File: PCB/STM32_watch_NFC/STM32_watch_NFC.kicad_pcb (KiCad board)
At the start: 4 copper layers, 37 x 37 mm, 119 parts, among them J1 Conn_01x06_Socket, J2 USB_C_Receptacle_PowerOnly_6P, Q1 2N7000, SW1 SW_DPST_x2, SW2 SW_DPST_x2, SW3 SW_DPST_x2, U1 STM32L031G6Ux, U2 MIC5365-3.3YC5, U3 TM1637, U4 MT3608, U5 BH1750FVI-TR, Y2 32.768kHz

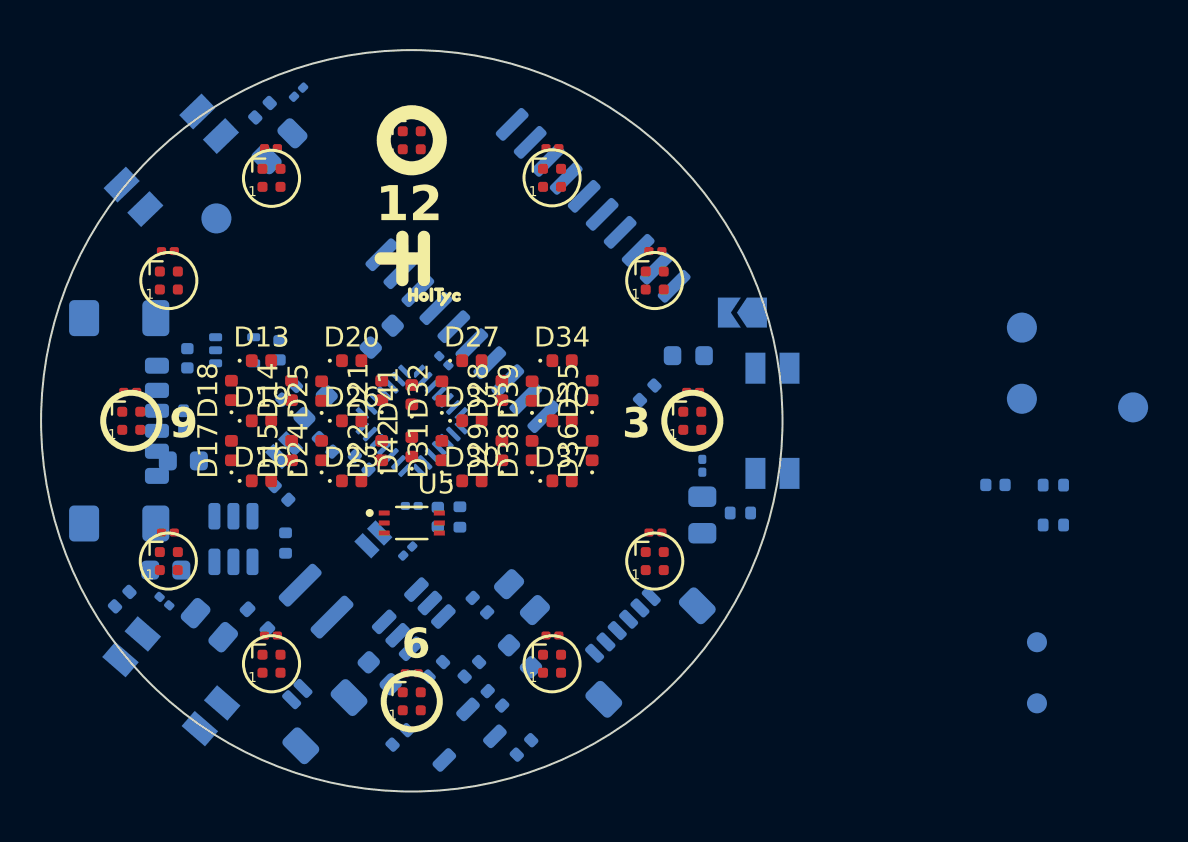
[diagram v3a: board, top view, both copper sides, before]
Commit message: TM1637 - in next commit I will delete the driver and connect the leds directly through matrix
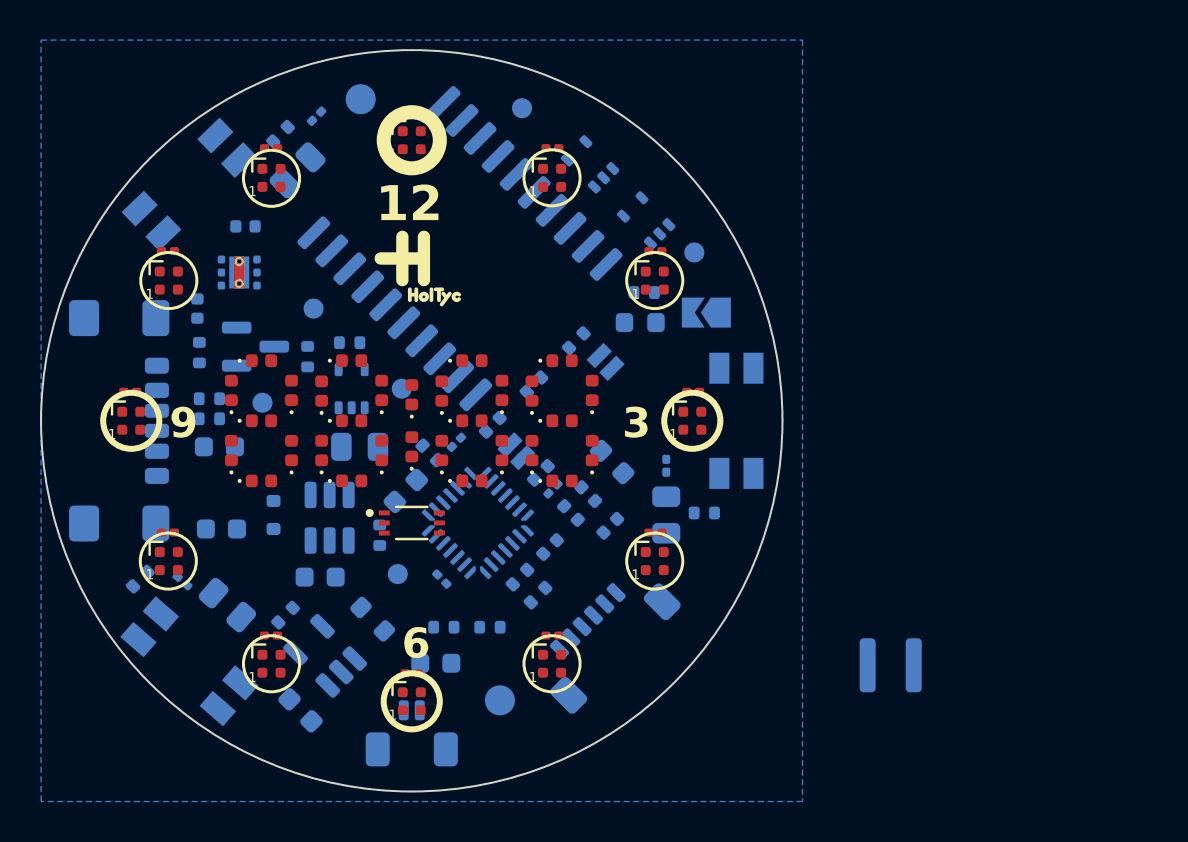
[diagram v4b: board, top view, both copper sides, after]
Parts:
- removed 3V3: 3V3, TestPoint:TestPoint_Pad_D1.5mm
- removed 5V1: 5V, TestPoint:TestPoint_Pad_D1.5mm
- removed C25: 10u, Capacitor_SMD:C_0603_1608Metric
- removed DINLED1, DINSTM2: ~, TestPoint:TestPoint_Pad_D1.0mm
- removed ME4055A1: ~, Package_TO_SOT_SMD:SOT-23-6
- removed U2: MIC5365-3.3YC5, Package_TO_SOT_SMD:SOT-353_SC-70-5
- added C32: 4.7uF, Capacitor_SMD:C_0603_1608Metric, B.Cu at (142.9, 119.4)
- added C33: 4.7uF, Capacitor_SMD:C_0603_1608Metric, B.Cu at (149.7, 117.1)
- added CLK: ~, TestPoint:TestPoint_Pad_D1.0mm, B.Cu at (162.6, 96.6)
- added DIO: ~, TestPoint:TestPoint_Pad_D1.0mm, B.Cu at (154.0, 89.4)
- added DLED: ~, TestPoint:TestPoint_Pad_D1.0mm, B.Cu at (148.0, 103.4)
- added DSTM: ~, TestPoint:TestPoint_Pad_D1.0mm, B.Cu at (141.1, 104.1)
- added R19: 5K1, Resistor_SMD:R_0402_1005Metric, B.Cu at (142.2, 114.7)
- added R22: 10k, Resistor_SMD:R_0603_1608Metric, B.Cu at (146.6, 114.9)
- added R23: 10K, Resistor_SMD:R_0402_1005Metric, B.Cu at (137.9, 101.6)
- added SCL: ~, TestPoint:TestPoint_Pad_D1.0mm, B.Cu at (147.8, 112.7)
- added SDA: ~, TestPoint:TestPoint_Pad_D1.0mm, B.Cu at (143.6, 99.4)
- added U10: LP5912-3.3DRV, Package_SON:WSON-6-1EP_2x2mm_P0.65mm_EP1x1.6mm_ThermalVias, B.Cu at (139.9, 97.6)
- added U6: MCP73831-3-OT, Package_TO_SOT_SMD:SOT-23-5, B.Cu at (144.2, 116.7)
- added U7: 74AHCT1G125, Package_TO_SOT_SMD:SOT-353_SC-70-5, B.Cu at (145.5, 103.4)
- added U8: 74AHCT1G125, Package_TO_SOT_SMD:SOT-353_SC-70-5, B.Cu at (160.2, 95.0)
- added U9: 74AHCT1G125, Package_TO_SOT_SMD:SOT-353_SC-70-5, B.Cu at (157.4, 92.2)
- L1: footprint Components:SLW3015 -> Inductor_SMD:L_Sunlord_SWPA3015S
- Q1: value 2N7000 -> BSS138; footprint Package_TO_SOT_SMD:TSOT-23 -> Package_TO_SOT_SMD:SOT-23
- R1, R2: value 10K -> 510
- R7: value 5K1 -> 10K
- moved GND 41.5 mm to (145.9, 89.0)
- moved +BAT 32.0 mm to (152.9, 119.0)
- moved L1 28.9 mm to (172.4, 117.2), turned to 180 degrees
- moved R21 26.7 mm to (153.9, 112.8), turned to -135 degrees
- moved R20 26.3 mm to (154.8, 113.7), turned to 45 degrees
- moved C31 22.4 mm to (155.4, 111.3), turned to 45 degrees
- moved Q1 22.3 mm to (140.7, 101.3), turned to 0 degrees
- moved R2 20.5 mm to (156.7, 101.0), turned to 45 degrees
- moved R6 19.9 mm to (145.4, 101.1), turned to 0 degrees
- moved C27 16.2 mm to (139.0, 110.4), turned to 180 degrees
- moved R1 15.8 mm to (154.6, 103.2), turned to -135 degrees
- moved C5 15.8 mm to (157.3, 108.7), turned to 135 degrees
- moved FB1 15.1 mm to (158.5, 107.1), turned to -45 degrees
- moved Y2 12.4 mm to (155.9, 104.3), turned to 45 degrees
- moved C8 11.1 mm to (152.5, 105.2), turned to 45 degrees
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- renumbered +BAT1 to +BAT, GND1 to GND
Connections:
- D13 pad 1: GRID1 -> A
- D13 pad 2: A -> GRID1
- D14 pad 1: GRID1 -> B
- D14 pad 2: B -> GRID1
- D15 pad 1: GRID1 -> C
- D15 pad 2: C -> GRID1
- D16 pad 1: GRID1 -> D
- D16 pad 2: D -> GRID1
- D17 pad 1: GRID1 -> E
- D17 pad 2: E -> GRID1
- D18 pad 1: GRID1 -> F
- D18 pad 2: F -> GRID1
- D19 pad 1: GRID1 -> G
- D19 pad 2: G -> GRID1
- D20 pad 1: GRID2 -> A
- D20 pad 2: A -> GRID2
- D21 pad 1: GRID2 -> B
- D21 pad 2: B -> GRID2
- D22 pad 1: GRID2 -> C
- D22 pad 2: C -> GRID2
- D23 pad 1: GRID2 -> D
- D23 pad 2: D -> GRID2
- D24 pad 1: GRID2 -> E
- D24 pad 2: E -> GRID2
- D25 pad 1: GRID2 -> F
- D25 pad 2: F -> GRID2
- D26 pad 1: GRID2 -> G
- D26 pad 2: G -> GRID2
- D27 pad 1: GRID3 -> A
- D27 pad 2: A -> GRID3
- D28 pad 1: GRID3 -> B
- D28 pad 2: B -> GRID3
- D29 pad 1: GRID3 -> C
- D29 pad 2: C -> GRID3
- D30 pad 1: GRID3 -> D
- D30 pad 2: D -> GRID3
- D31 pad 1: GRID3 -> E
- D31 pad 2: E -> GRID3
- D32 pad 1: GRID3 -> F
- D32 pad 2: F -> GRID3
- D33 pad 1: GRID3 -> G
- D33 pad 2: G -> GRID3
- D34 pad 1: GRID4 -> A
- D34 pad 2: A -> GRID4
- D35 pad 1: GRID4 -> B
- D35 pad 2: B -> GRID4
- D36 pad 1: GRID4 -> C
- D36 pad 2: C -> GRID4
- D37 pad 1: GRID4 -> D
- D37 pad 2: D -> GRID4
- D38 pad 1: GRID4 -> E
- D38 pad 2: E -> GRID4
- D39 pad 1: GRID4 -> F
- D39 pad 2: F -> GRID4
- D40 pad 1: GRID4 -> G
- D40 pad 2: G -> GRID4
- D41 pad 1: GND -> Net-(D41-K)
- D42 pad 1: GND -> Net-(D42-K)
- Q1 pad 1: DIN_STM -> VBUS
- Q1 pad 2: +3.3V -> GND
- Q1 pad 3: DIN_LED -> CHRG_STM
- R1 pad 1: +3.3V -> GND
- R1 pad 2: DIN_STM -> Net-(D42-K)
- R2 pad 1: +5V -> Net-(D41-K)
- R2 pad 2: DIN_LED -> GND
- R6 pad 1: DIN_STM -> DIN_LED
- R7 pad 1: Net-(ME4055A1-PROG) -> +3.3V
- R7 pad 2: GND -> CHRG_STM
- U1 pad 13: unconnected-(U1-PA7-Pad13) -> CLK_TM_STM
- U1 pad 14: unconnected-(U1-PB0-Pad14) -> DIO_TM_STM
- U3 pad 17: unconnected-(U3-DIO-Pad17) -> DIO_TM
- U3 pad 18: unconnected-(U3-CLK-Pad18) -> CLK_TM
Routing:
- added copper zone on B.Cu, net GND
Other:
- board text added: "Rev.B.1"
- board text removed: "+"
- board text removed: "Rev.B.0"

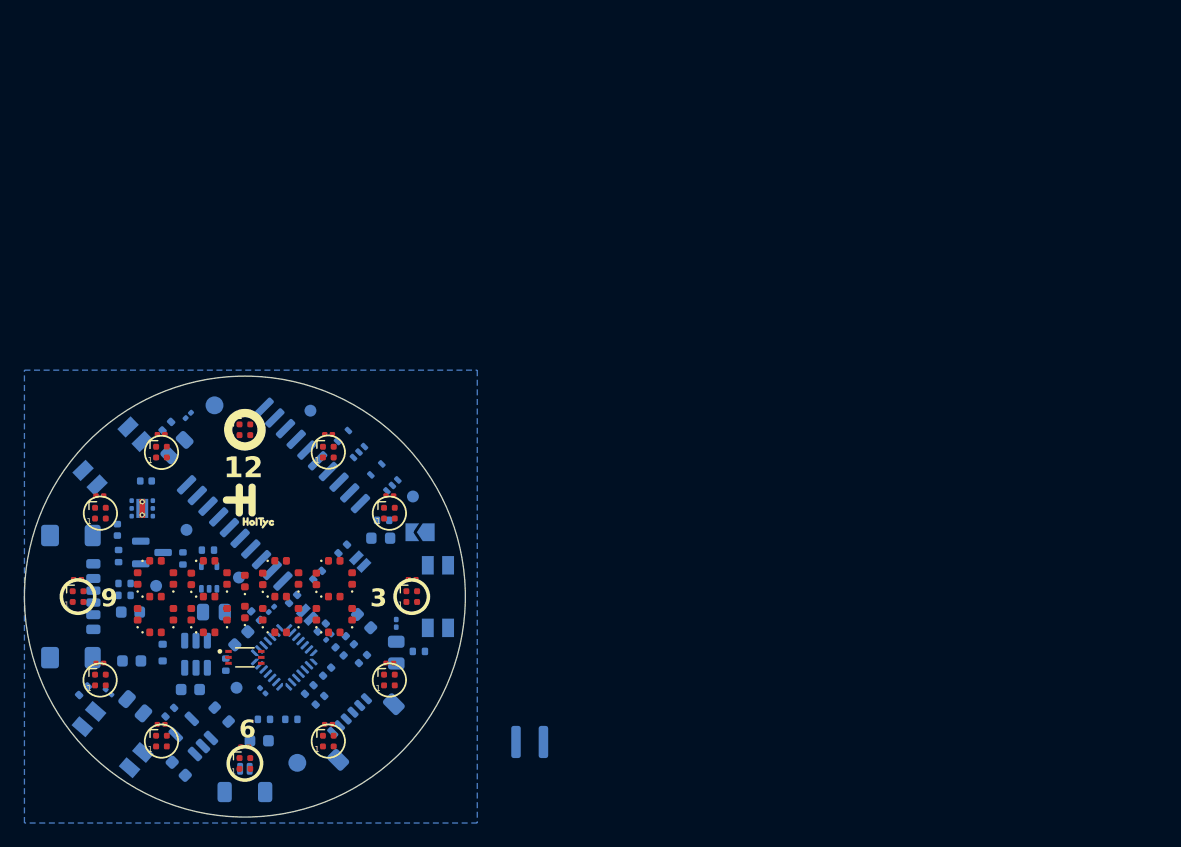
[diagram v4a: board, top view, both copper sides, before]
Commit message: Kicad/STM - new Routing 6
Version before Boston to work on it there - needs to replace every component :(
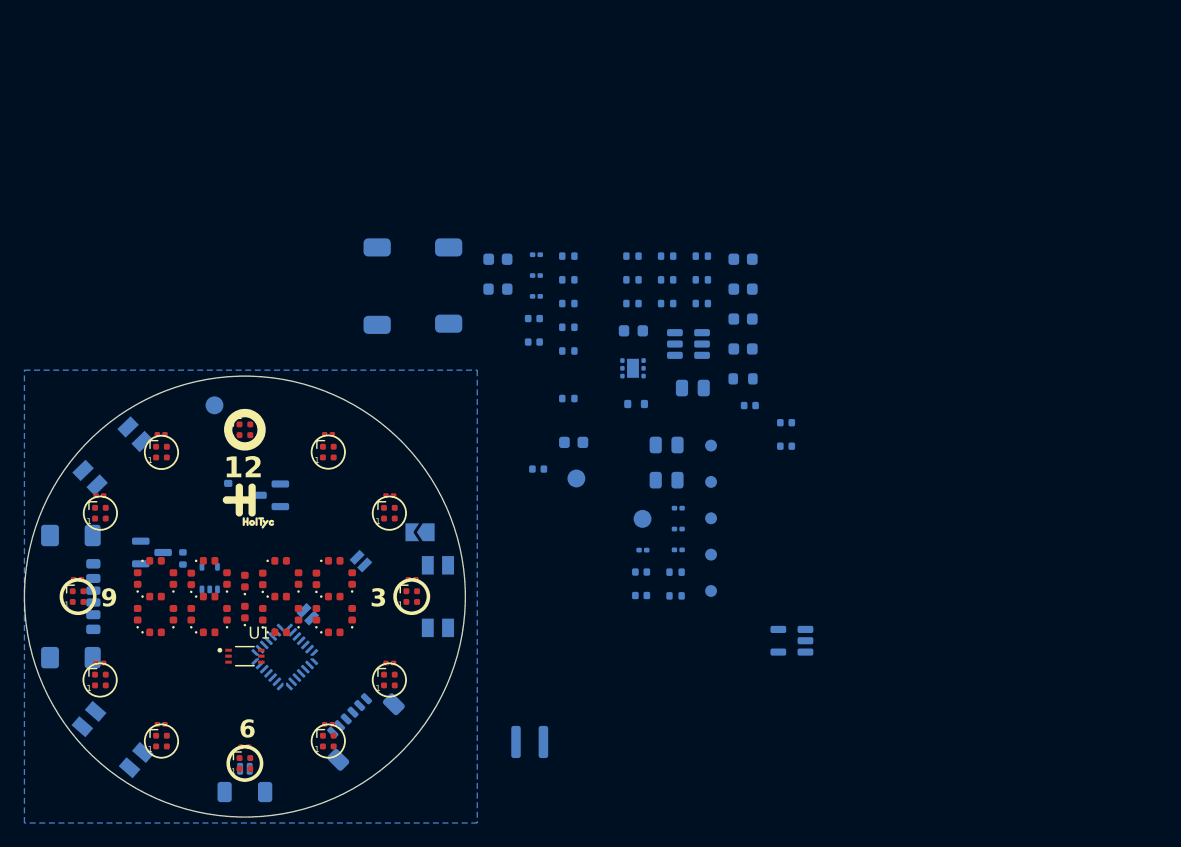
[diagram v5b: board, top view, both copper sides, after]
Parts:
- removed +BAT: 2.7-4.2V, TestPoint:TestPoint_Pad_D1.5mm
- removed the C24 at (138.9, 106.3)
- removed C33: 4.7uF, Capacitor_SMD:C_0603_1608Metric
- removed CLK, DIO, DLED, DSTM, SCL, SDA: ~, TestPoint:TestPoint_Pad_D1.0mm
- removed R23: 10K, Resistor_SMD:R_0402_1005Metric
- removed U10: LP5912-3.3DRV, Package_SON:WSON-6-1EP_2x2mm_P0.65mm_EP1x1.6mm_ThermalVias
- removed U7, U8, U9: 74AHCT1G125, Package_TO_SOT_SMD:SOT-353_SC-70-5
- removed Y2: 32.768kHz, Crystal:Crystal_SMD_SeikoEpson_MC146-4Pin_6.7x1.5mm
- added +BAT1: 2.7-4.2V, TestPoint:TestPoint_Pad_D1.5mm, B.Cu at (176.3, 95.1)
- added BZ1: Buzzer, Buzzer_SMD:Buzzer_SMD, B.Cu at (162.6, 78.9)
- added Buzzer_d1: ~, TestPoint:TestPoint_Pad_D1.0mm, B.Cu at (187.6, 92.3)
- added C12: 15pF, Capacitor_SMD:C_0402_1005Metric, B.Cu at (193.9, 90.4)
- added C13: 15pF, Capacitor_SMD:C_0402_1005Metric, B.Cu at (193.9, 92.4)
- added C25: 100n, Capacitor_SMD:C_0201_0603Metric, B.Cu at (181.9, 101.1)
- added D45: D_Schottky, Diode_SMD:D_SOD-523, B.Cu at (181.3, 88.8)
- added DINLED1: ~, TestPoint:TestPoint_Pad_D1.0mm, B.Cu at (187.6, 95.4)
- added DINSTM1: ~, TestPoint:TestPoint_Pad_D1.0mm, B.Cu at (187.6, 98.4)
- added GND1: GND, TestPoint:TestPoint_Pad_D1.5mm, B.Cu at (181.9, 98.5)
- added Q2: AO3400A, Package_TO_SOT_SMD:SOT-23, B.Cu at (140.7, 101.3)
- added SCL_L1: ~, TestPoint:TestPoint_Pad_D1.0mm, B.Cu at (187.6, 101.5)
- added SDA_L1: ~, TestPoint:TestPoint_Pad_D1.0mm, B.Cu at (187.6, 104.5)
- added U2: 74AHCT1G125, Package_TO_SOT_SMD:SOT-353_SC-70-5, B.Cu at (145.6, 103.5)
- added Y1: 32.768kHz, Crystal:Crystal_SMD_SeikoEpson_MC146-4Pin_6.7x1.5mm, B.Cu at (156.0, 104.3)
- C11, C6: value 1u -> 100n; footprint Capacitor_SMD:C_0402_1005Metric -> Capacitor_SMD:C_0201_0603Metric
- C2, C28: value 100n -> 1u; footprint Capacitor_SMD:C_0201_0603Metric -> Capacitor_SMD:C_0402_1005Metric
- C27: value 10u -> 1u; footprint Capacitor_SMD:C_0603_1608Metric -> Capacitor_SMD:C_0402_1005Metric
- C29, C30: value 100n -> 4.7uF; footprint Capacitor_SMD:C_0201_0603Metric -> Capacitor_SMD:C_0603_1608Metric
- C3: value 10n -> 100n; footprint Capacitor_SMD:C_0402_1005Metric -> Capacitor_SMD:C_0201_0603Metric
- C31, C5: value 1u -> 10u; footprint Capacitor_SMD:C_0402_1005Metric -> Capacitor_SMD:C_0603_1608Metric
- C32: value 4.7uF -> 10u
- C4: value 10u -> 100n; footprint Capacitor_SMD:C_0603_1608Metric -> Capacitor_SMD:C_0201_0603Metric
- C8: value 15pF -> 10n
- C9: value 15pF -> 1u
- Q1: value BSS138 -> BC817
- R10, R14: value 16.5K -> 10K; footprint Resistor_SMD:R_0805_2012Metric -> Resistor_SMD:R_0402_1005Metric
- R12: value 16.5K -> 510; footprint Resistor_SMD:R_0805_2012Metric -> Resistor_SMD:R_0402_1005Metric
- R13, R20: value 510 -> 10K
- R15: value 510 -> 5K1
- R16: value 10K -> 5K1
- R18: value 510 -> 16.5K; footprint Resistor_SMD:R_0402_1005Metric -> Resistor_SMD:R_0805_2012Metric
- R21: value 510 -> 10k; footprint Resistor_SMD:R_0402_1005Metric -> Resistor_SMD:R_0603_1608Metric
- R22: value 10k -> 2.2K; footprint Resistor_SMD:R_0603_1608Metric -> Resistor_SMD:R_0402_1005Metric
- R3: value 10K -> 16.5K; footprint Resistor_SMD:R_0402_1005Metric -> Resistor_SMD:R_0805_2012Metric
- R4: value 5K1 -> 510
- R5: value 5K1 -> 16.5K; footprint Resistor_SMD:R_0402_1005Metric -> Resistor_SMD:R_0805_2012Metric
- R7: value 10K -> 16.5K
- R8: value 16.5K -> 5K1; footprint Resistor_SMD:R_0805_2012Metric -> Resistor_SMD:R_0402_1005Metric
- R9: value 2.2K -> 510
- U1: value STM32L031G6Ux -> BH1750FVI-TR; footprint Package_DFN_QFN:QFN-28_4x4mm_P0.5mm -> BH1750FVI-TR:XDCR_BH1750FVI-TR; moved to F.Cu
- U3: value TM1637 -> STM32L031G6Ux; footprint Package_SO:SOP-20_7.5x12.8mm_P1.27mm -> Package_DFN_QFN:QFN-28_4x4mm_P0.5mm
- U4: value MT3608 -> LP5912-3.3DRV; footprint Package_TO_SOT_SMD:SOT-23-6 -> Package_SON:WSON-6-1EP_2x2mm_P0.65mm_EP1x1.6mm
- U5: value BH1750FVI-TR -> MCP73831-3-OT; footprint BH1750FVI-TR:XDCR_BH1750FVI-TR -> Package_TO_SOT_SMD:SOT-23-5; moved to B.Cu
- U6: value MCP73831-3-OT -> MT3608; footprint Package_TO_SOT_SMD:SOT-23-5 -> Package_TO_SOT_SMD:SOT-23-6
- moved C29 64.4 mm to (190.3, 76.7), turned to 180 degrees
- moved R13 62.3 mm to (186.8, 78.4), turned to 180 degrees
- moved R12 60.7 mm to (186.8, 76.4), turned to 180 degrees
- moved C32 59.0 mm to (190.3, 84.2), turned to 180 degrees
- moved R19 54.5 mm to (181.0, 76.4), turned to 180 degrees
- moved U6 53.0 mm to (185.7, 83.8), turned to 180 degrees
- moved R16 50.0 mm to (183.9, 78.4), turned to 180 degrees
- moved R22 48.8 mm to (181.0, 80.4), turned to 180 degrees
- moved C28 47.1 mm to (190.9, 89.0), turned to 180 degrees
- moved C11 47.1 mm to (184.9, 101.1), turned to 180 degrees
- moved R17 47.0 mm to (183.9, 80.4), turned to 180 degrees
- moved R5 46.3 mm to (183.9, 95.2)
- moved R4 46.3 mm to (184.6, 103.0), turned to 180 degrees
- moved U5 45.9 mm to (194.4, 108.7), turned to 180 degrees
- moved C31 45.8 mm to (190.3, 81.7), turned to 180 degrees
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- renumbered C12 to C14, C13 to C15, C14 to C16, C15 to C17, C16 to C18, C17 to C19, C18 to C20, C19 to C21, C20 to C22, C21 to C23, C22 to C24, C23 to C25
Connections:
- C1 pad 1: +3.3V -> GND
- C1 pad 2: GND -> Button_LT
- C10 pad 2: +5V -> +3.3V
- C11 pad 1: GND -> /NRST
- C11 pad 2: +3.3V -> GND
- C2 pad 1: +3.3V -> Net-(U1-DVI)
- C26 pad 1: +BATT -> VBUS
- C27 pad 1: +5V -> GND
- C27 pad 2: GND -> +5V
- C28 pad 2: Button_LT -> +3.3V
- C29 pad 1: GND -> VBUS
- C29 pad 2: Button_LB -> GND
- C3 pad 1: +3.3VA -> GND
- C3 pad 2: GND -> Button_LB
- C30 pad 2: Button_R -> +BATT
- C31 pad 1: Net-(U5-DVI) -> +5V
- C32 pad 1: Vbus_1 -> +BATT
- C4 pad 1: +3.3V -> GND
- C4 pad 2: GND -> Button_R
- C5 pad 1: GND -> +3.3V
- C5 pad 2: +3.3VA -> GND
- C6 pad 1: GND -> +3.3V
- C6 pad 2: +3.3V -> GND
- C7 pad 1: /NRST -> +3.3V
- C8 pad 1: /LSE_IN -> +3.3VA
- C9 pad 1: /LSE_OUT -> GND
- C9 pad 2: GND -> +3.3VA
- D13 pad 1: A -> Row1
- D13 pad 2: GRID1 -> Row2
- D14 pad 1: B -> Row1
- D14 pad 2: GRID1 -> Row3
- D15 pad 1: C -> Row1
- D15 pad 2: GRID1 -> Row4
- D16 pad 1: D -> Row1
- D16 pad 2: GRID1 -> Row5
- D17 pad 1: E -> Row1
- D17 pad 2: GRID1 -> Row6
- D18 pad 1: F -> Row2
- D18 pad 2: GRID1 -> Row1
- D19 pad 1: G -> Row2
- D19 pad 2: GRID1 -> Row3
- D20 pad 1: A -> Row2
- D20 pad 2: GRID2 -> Row4
- D21 pad 1: B -> Row2
- D21 pad 2: GRID2 -> Row5
- D22 pad 1: C -> Row2
- D22 pad 2: GRID2 -> Row6
- D23 pad 1: D -> Row3
- D23 pad 2: GRID2 -> Row1
- D24 pad 1: E -> Row3
- D24 pad 2: GRID2 -> Row2
- D25 pad 1: F -> Row3
- D25 pad 2: GRID2 -> Row4
- D26 pad 1: G -> Row3
- D26 pad 2: GRID2 -> Row5
- D27 pad 1: A -> Row3
- D27 pad 2: GRID3 -> Row6
- D28 pad 1: B -> Row4
- D28 pad 2: GRID3 -> Row1
- D29 pad 1: C -> Row4
- D29 pad 2: GRID3 -> Row2
- D30 pad 1: D -> Row4
- D30 pad 2: GRID3 -> Row3
- D31 pad 1: E -> Row4
- D31 pad 2: GRID3 -> Row5
- D32 pad 1: F -> Row4
- D32 pad 2: GRID3 -> Row6
- D33 pad 1: G -> Row5
- D33 pad 2: GRID3 -> Row1
- D34 pad 1: A -> Row5
- D34 pad 2: GRID4 -> Row2
- D35 pad 1: B -> Row5
- D35 pad 2: GRID4 -> Row3
- D36 pad 1: C -> Row5
- D36 pad 2: GRID4 -> Row4
- D37 pad 1: D -> Row5
- D37 pad 2: GRID4 -> Row6
- D38 pad 1: E -> Row6
- D38 pad 2: GRID4 -> Row1
- D39 pad 1: F -> Row6
- D39 pad 2: GRID4 -> Row2
- D40 pad 1: G -> Row6
- D40 pad 2: GRID4 -> Row3
- D41 pad 1: Net-(D41-K) -> Row6
- D41 pad 2: LED_tecka_2 -> Row4
- D42 pad 1: Net-(D42-K) -> Row6
- D42 pad 2: LED_tecka_1 -> Row5
- D43 pad 1: +5V -> +3.3V
- D43 pad 2: Net-(D43-A) -> Net-(BZ1--)
- L1 pad 2: Net-(D43-A) -> Net-(D45-A)
- Q1 pad 1: VBUS -> Net-(Q1-B)
- Q1 pad 3: CHRG_STM -> Net-(BZ1--)
- R1 pad 1: GND -> Net-(R1-Pad1)
- R1 pad 2: Net-(D42-K) -> +3.3V
- R10 pad 1: Button_LT -> GND
- R10 pad 2: GND -> Net-(U3-BOOT0)
- R11 pad 1: Net-(SW3A-A) -> DIN_LED
- R11 pad 2: Button_LT -> Net-(D1-DIN)
- R12 pad 1: Button_LB -> Net-(D44-K)
- R13 pad 1: Net-(SW1A-A) -> +BATT
- R13 pad 2: Button_LB -> BATT_STM
- R14 pad 1: Button_R -> BATT_STM
- R15 pad 1: Net-(SW2A-A) -> Net-(J2-CC1)
- R15 pad 2: Button_R -> GND
- R16 pad 1: +BATT -> GND
- R16 pad 2: BATT_STM -> Net-(J2-CC2)
- R17 pad 1: BATT_STM -> +3.3V
- R17 pad 2: GND -> CHRG_STM
- R18 pad 1: Net-(D44-K) -> +5V
- R18 pad 2: GND -> Net-(U6-FB)
- R19 pad 2: Net-(U6-PROG) -> Net-(U5-PROG)
- R2 pad 1: Net-(D41-K) -> Net-(U1-DVI)
- R2 pad 2: GND -> Net-(R1-Pad1)
- R20 pad 1: Net-(R20-Pad1) -> VBUS
- R20 pad 2: +3.3V -> GND
- R21 pad 1: Net-(U5-DVI) -> DONE_STM
- R21 pad 2: Net-(R20-Pad1) -> VBUS
- R22 pad 1: DONE_STM -> Net-(U6-FB)
- R22 pad 2: VBUS -> GND
- R3 pad 1: GND -> Button_LT
- R3 pad 2: Net-(U1-BOOT0) -> GND
- R4 pad 1: Net-(J2-CC1) -> Net-(SW3A-A)
- R4 pad 2: GND -> Button_LT
- R5 pad 1: GND -> Button_LB
- R5 pad 2: Net-(J2-CC2) -> GND
- R6 pad 1: DIN_LED -> Net-(SW1A-A)
- R6 pad 2: Net-(D1-DIN) -> Button_LB
- R7 pad 1: +3.3V -> Button_R
- R7 pad 2: CHRG_STM -> GND
- R8 pad 1: +5V -> Buzzer
- R8 pad 2: Net-(U4-FB) -> Net-(Q1-B)
- R9 pad 1: Net-(U4-FB) -> Net-(SW2A-A)
- R9 pad 2: GND -> Button_R
- U1 pad 2: /LSE_IN -> GND
- U1 pad 3: /LSE_OUT -> GND
- U1 pad 4: /NRST -> SDA_LIGHT
- U1 pad 5: +3.3VA -> Net-(U1-DVI)
- U1 pad 6: Button_LT -> SCL_LIGHT
- U3 pad 1: GND -> +3.3V
- U3 pad 10: unconnected-(U3-GRID6-Pad10) -> Row3
- U3 pad 11: unconnected-(U3-GRID5-Pad11) -> Row4
- U3 pad 12: GRID4 -> Row5
- U3 pad 13: GRID3 -> Row6
- U3 pad 14: GRID2 -> unconnected-(U3-PB0-Pad14)
- U3 pad 15: GRID1 -> BATT_STM
- U3 pad 16: +5V -> GND
- U3 pad 17: DIO_TM -> +3.3V
- U3 pad 18: CLK_TM -> CHRG_STM
- U3 pad 19: unconnected-(U3-K1-Pad19) -> DONE_STM
- U3 pad 2: A -> /LSE_IN
- U3 pad 20: unconnected-(U3-K2-Pad20) -> Button_R
- U3 pad 3: B -> /LSE_OUT
- U3 pad 4: C -> /NRST
- U3 pad 5: D -> +3.3VA
- U3 pad 6: E -> Button_LT
- U3 pad 7: F -> Button_LB
- U3 pad 8: G -> Row1
- U3 pad 9: unconnected-(U3-SEG8/KS8-Pad9) -> Row2
- U4 pad 1: Net-(D43-A) -> +3.3V
- U4 pad 2: GND -> unconnected-(U4-NC-Pad2)
- U4 pad 3: Net-(U4-FB) -> GND
- U4 pad 4: +BATT -> +5V
- U4 pad 5: +BATT -> GND
- U4 pad 6: unconnected-(U4-NC-Pad6) -> +5V
- U5 pad 1: +3.3V -> DONE_STM
- U5 pad 3: GND -> +BATT
- U5 pad 4: SDA_LIGHT -> VBUS
- U5 pad 5: Net-(U5-DVI) -> Net-(U5-PROG)
- U6 pad 1: DONE_STM -> Net-(D45-A)
- U6 pad 3: +BATT -> Net-(U6-FB)
- U6 pad 4: Vbus_1 -> +BATT
- U6 pad 5: Net-(U6-PROG) -> +BATT

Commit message: REBORN - new design lead
We have new vision for watches future so we will see
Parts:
- removed D41, D42: LED, LED_SMD:LED_0402_1005Metric
- moved +BAT1 30.0 mm to (205.2, 86.8)
- moved C10 30.0 mm to (210.6, 96.7)
- moved C12 30.0 mm to (222.8, 82.2)
- moved C13 30.0 mm to (222.8, 84.1)
- moved C2 30.0 mm to (210.6, 94.7)
- moved C25 30.0 mm to (210.7, 92.8)
- moved C27 30.0 mm to (201.9, 86.0)
- moved C28 30.0 mm to (219.7, 80.7)
- moved C29 30.0 mm to (219.1, 68.4)
- moved C3 30.0 mm to (201.8, 68.1)
- moved C30 30.0 mm to (219.1, 70.9)
- moved C31 30.0 mm to (219.1, 73.5)
- moved C32 30.0 mm to (219.1, 76.0)
- moved C5 30.0 mm to (198.6, 68.4)
- moved C6 30.0 mm to (201.8, 69.8)
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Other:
- board text removed: "12"
- board text removed: "3"
- board text removed: "6"
- board text removed: "9"

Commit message: Component placement
I placed every component in logical way
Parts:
- removed the C25 at (210.7, 92.8)
- removed D44: LED, LED_SMD:LED_0603_1608Metric
- removed G***: LOGO, LOGO
- removed GND, GND1: GND, TestPoint:TestPoint_Pad_D1.5mm
- removed JP1: SolderJumper_2_Open, Jumper:SolderJumper-2_P1.3mm_Open_TrianglePad1.0x1.5mm
- removed R1, R12, R2: 510, Resistor_SMD:R_0402_1005Metric
- added R23: 2.2K, Resistor_SMD:R_0402_1005Metric, F.Cu at (143.3, 104.2)
- C2: moved to F.Cu
- moved R17 83.5 mm to (140.8, 114.4), turned to 45 degrees
- moved C12 83.3 mm to (145.8, 114.0), turned to 135 degrees
- moved R15 83.3 mm to (138.5, 105.8), turned to 0 degrees
- moved C29 83.3 mm to (144.1, 104.5), turned to -90 degrees
- moved R16 81.9 mm to (138.5, 104.6)
- moved C28 81.8 mm to (140.3, 100.4), turned to -90 degrees
- moved R20 80.6 mm to (140.0, 110.2), turned to 45 degrees
- moved C13 79.4 mm to (147.9, 110.8), turned to 135 degrees
- moved C31 79.3 mm to (143.4, 97.0), turned to 0 degrees
- moved R4 79.1 mm to (134.4, 96.8), turned to -45 degrees
- moved R6 78.8 mm to (141.6, 119.6), turned to 45 degrees
- moved C32 77.9 mm to (142.6, 90.4), turned to -90 degrees
- moved DINL 77.5 mm to (145.6, 118.6)
- moved C3 76.8 mm to (143.4, 118.0), turned to -135 degrees
- moved C1 76.8 mm to (137.4, 98.0), turned to 135 degrees
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- renumbered +BAT1 to BAT, Buzzer_d1 to Buz, DINLED1 to DINL, DINSTM1 to DINS, SCL_L1 to SCL, SDA_L1 to SDA
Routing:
- net +3.3V: track 0.00 -> 15.9 mm
- net Net-(SW1A-A): track 0.00 -> 5.39 mm
- net Net-(SW3A-A): track 0.00 -> 5.29 mm
- net Net-(SW2A-A): track 0.00 -> 5.25 mm

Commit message: Routing #1
Starting routing
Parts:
- added G***: LOGO, LOGO, F.Cu at (148.8, 98.5)
- moved C2 10.3 mm to (151.2, 110.4), turned to -90 degrees
- moved D17 7.79 mm to (138.2, 106.5)
- moved D18 7.79 mm to (138.2, 103.5)
- moved D16 7.76 mm to (139.9, 108.2)
- moved D19 7.62 mm to (139.9, 105.0)
- moved D35 7.61 mm to (158.5, 103.5)
- moved D36 7.61 mm to (158.5, 106.5)
- moved D34 7.54 mm to (156.7, 101.8)
- moved D13 7.48 mm to (139.9, 101.8)
- moved D40 7.39 mm to (156.7, 105.0)
- moved D14 7.37 mm to (141.8, 103.5)
- moved D15 7.37 mm to (141.8, 106.5)
- moved D24 7.37 mm to (143.2, 106.5)
- moved D25 7.35 mm to (143.2, 103.5)
- moved D23 7.33 mm to (145.0, 108.2)
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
